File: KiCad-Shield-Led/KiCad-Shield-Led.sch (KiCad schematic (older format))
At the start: 16 parts, among them P1 Power, P2 Analog, P3 Digital, P4 Digital, P5 CONN_01X01, P6 CONN_01X01, P7 CONN_01X01, P8 CONN_01X01

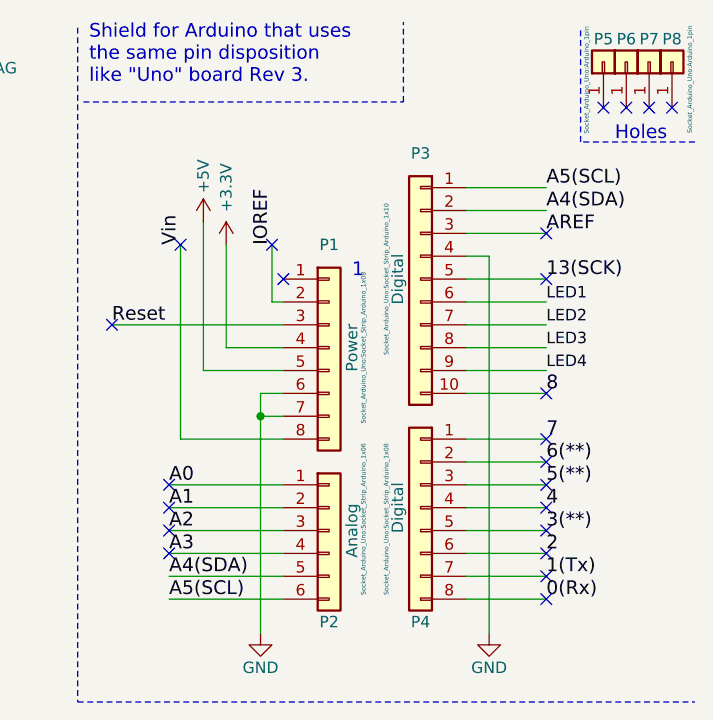
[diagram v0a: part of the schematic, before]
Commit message: Routage des signaux de la carte
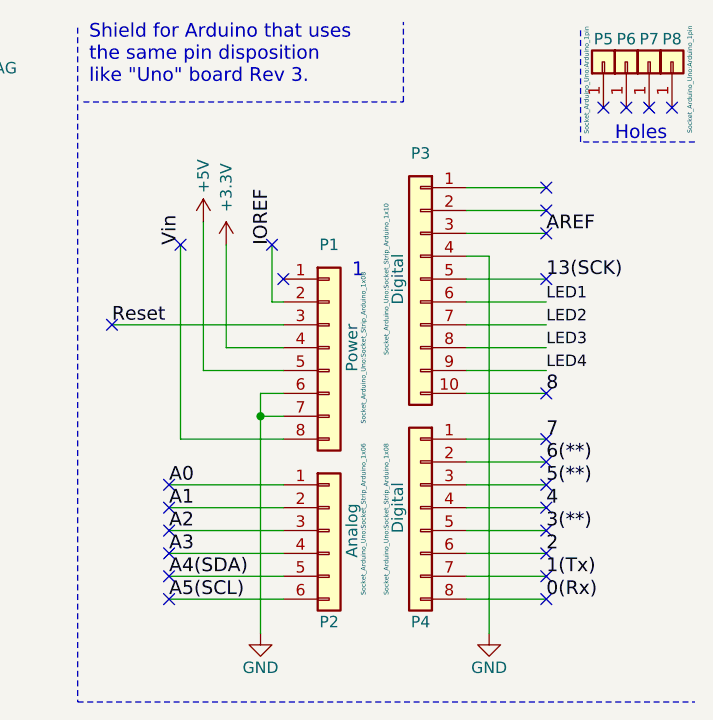
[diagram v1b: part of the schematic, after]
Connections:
- net A4(SDA): no longer P3.2 (Pin_2)
- net A5(SCL): no longer P3.1 (Pin_1)
- no-connect marks 23 -> 27
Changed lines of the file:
@@
 AREF
 NoConn ~ 9400 1600
-Text Label 10550 1300 0    60   ~ 0
-A4(SDA)
-Text Label 10550 1200 0    60   ~ 0
-A5(SCL)
 Text Notes 10850 1000 0    60   ~ 0
 Holes
@@
 Wire Wire Line
 	6550 2100 6550 1700
-Wire Wire Line
-	6550 1700 7950 1700
-Text Label 7950 1700 0    50   ~ 0
-LED1
-Text Label 7950 1800 0    50   ~ 0
-LED2
 Text Label 7950 1900 0    50   ~ 0
 LED3
@@
 Text Label 10550 1700 0    50   ~ 0
 LED1
-Text Label 10550 1800 0    50   ~ 0
-LED2
 Text Label 10550 1900 0    50   ~ 0
 LED3
@@
 	1    0    0    -1
 $EndComp
+Text Label 10550 1800 0    50   ~ 0
+LED2
+Text Label 7950 1800 0    50   ~ 0
+LED2
+Text Label 7950 1700 0    50   ~ 0
+LED1
+Wire Wire Line
+	6550 1700 7950 1700
+NoConn ~ 10550 1200
+NoConn ~ 10550 1300
+NoConn ~ 8900 2900
+NoConn ~ 8900 3000
 $EndSCHEMATC

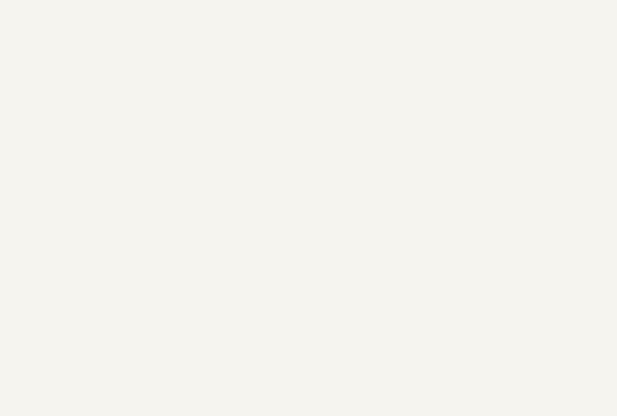
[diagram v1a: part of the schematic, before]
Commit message: Ajout du modele 3D de notre librairie GazSensor
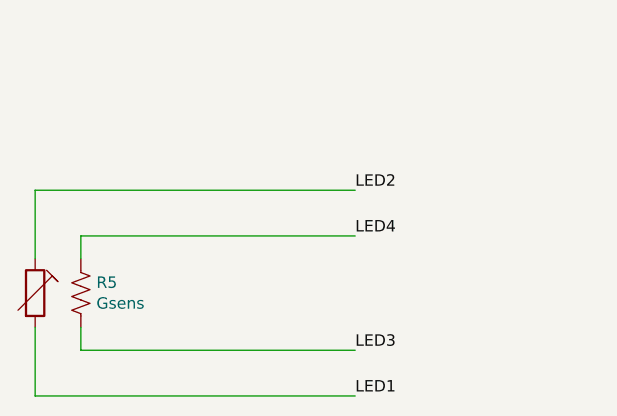
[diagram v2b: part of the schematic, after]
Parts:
- added R5: Gsens, MesEmpreintes:TO-5-10_Window, symbol iss_gpB_gazSensor:Gsens
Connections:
- net LED1: now also R5.1
- net LED2: now also R5.2
- net LED3: now also R5.3
- net LED4: now also R5.4
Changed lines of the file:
@@
 NoConn ~ 8900 2900
 NoConn ~ 8900 3000
+$Comp
+L iss_gpB_gazSensor:Gsens R5
+U 1 1 5FCB75C6
+P 3600 3350
+F 0 "R5" H 3768 3396 50  0000 L CNN
+F 1 "Gsens" H 3768 3305 50  0000 L CNN
+F 2 "MesEmpreintes:TO-5-10_Window" V 3430 3350 50  0001 C CNN
+F 3 "~" H 3500 3350 50  0001 C CNN
+	1    3600 3350
+	1    0    0    -1
+$EndComp
+Text Label 4900 3600 0    50   ~ 0
+LED3
+Text Label 4900 3100 0    50   ~ 0
+LED4
+Text Label 4900 2900 0    50   ~ 0
+LED2
+Text Label 4900 3800 0    50   ~ 0
+LED1
+Wire Wire Line
+	3500 3800 4900 3800
+Wire Wire Line
+	3500 2900 3500 3200
+Wire Wire Line
+	3500 2900 4900 2900
+Wire Wire Line
+	3700 3100 3700 3200
+Wire Wire Line
+	3700 3100 4900 3100
+Wire Wire Line
+	3700 3600 3700 3500
+Wire Wire Line
+	3700 3600 4900 3600
+Wire Wire Line
+	3500 3800 3500 3500
 $EndSCHEMATC
